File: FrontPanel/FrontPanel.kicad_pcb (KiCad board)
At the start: 2 copper layers, 72 parts, among them SW1 Channel 1, SW10 5, SW11 2, SW12 0, SW13 9, SW14 6, SW15 3, SW16 Backspace, SW17 Voltage 1, SW18 Current 1, SW19 Voltage 2, SW2 Confirm, SW20 Current 2, SW3 Cancel, SW4 Channel 2, SW5 7, SW6 4, SW7 1, SW8 Decimal, SW9 8

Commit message: Fix front panel and routed main regulator
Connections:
- C_DBC_21 pad 1: Net-(Front_Panel2-Pad1) -> Net-(C_DBC_21-Pad1)
- C_DBC_22 pad 2: Net-(Front_Panel2-Pad1) -> Net-(C_DBC_21-Pad1)
- C_DBC_23 pad 1: Net-(Front_Panel2-Pad6) -> Net-(C_DBC_23-Pad1)
- C_DBC_23 pad 2: Net-(C_DBC_23-Pad2) -> Net-(RotaryEncoder+Switch1-PadS2)
- Front_Panel2 pad 1: Net-(Front_Panel2-Pad1) -> Net-(C_DBC_21-Pad1)
- Front_Panel2 pad 13: Net-(SW1-Pad1) -> Net-(SW13-Pad1)
- Front_Panel2 pad 14: Net-(SW10-Pad1) -> Net-(Front_Panel2-Pad14)
- Front_Panel2 pad 15: Net-(SW11-Pad1) -> Net-(Front_Panel2-Pad15)
- Front_Panel2 pad 16: Net-(SW12-Pad1) -> Net-(Front_Panel2-Pad16)
- R1 pad 2: Net-(Front_Panel2-Pad1) -> Net-(C_DBC_21-Pad1)
- R2 pad 2: Net-(Front_Panel2-Pad1) -> Net-(C_DBC_21-Pad1)
- R_DBC_1 pad 1: Net-(C_DBC_1-Pad2) -> Net-(SW13-Pad1)
- R_DBC_10 pad 1: Net-(C_DBC_10-Pad2) -> Net-(Front_Panel2-Pad14)
- R_DBC_11 pad 1: Net-(C_DBC_10-Pad2) -> Net-(Front_Panel2-Pad15)
- R_DBC_12 pad 1: Net-(C_DBC_10-Pad2) -> Net-(Front_Panel2-Pad16)
- R_DBC_13 pad 1: Net-(C_DBC_13-Pad2) -> Net-(SW13-Pad1)
- R_DBC_14 pad 1: Net-(C_DBC_13-Pad2) -> Net-(Front_Panel2-Pad14)
- R_DBC_15 pad 1: Net-(C_DBC_13-Pad2) -> Net-(Front_Panel2-Pad15)
- R_DBC_16 pad 1: Net-(C_DBC_13-Pad2) -> Net-(Front_Panel2-Pad16)
- R_DBC_17 pad 1: Net-(C_DBC_17-Pad2) -> Net-(SW13-Pad1)
- R_DBC_18 pad 1: Net-(C_DBC_17-Pad2) -> Net-(Front_Panel2-Pad14)
- R_DBC_19 pad 1: Net-(C_DBC_17-Pad2) -> Net-(Front_Panel2-Pad15)
- R_DBC_2 pad 1: Net-(C_DBC_1-Pad2) -> Net-(Front_Panel2-Pad14)
- R_DBC_20 pad 1: Net-(C_DBC_17-Pad2) -> Net-(Front_Panel2-Pad16)
- R_DBC_23 pad 1: Net-(C_DBC_23-Pad2) -> Net-(C_DBC_21-Pad1)
- R_DBC_23 pad 2: Net-(Front_Panel2-Pad6) -> Net-(C_DBC_23-Pad1)
- R_DBC_3 pad 1: Net-(C_DBC_1-Pad2) -> Net-(Front_Panel2-Pad15)
- R_DBC_4 pad 1: Net-(C_DBC_1-Pad2) -> Net-(Front_Panel2-Pad16)
- R_DBC_5 pad 1: Net-(C_DBC_5-Pad2) -> Net-(SW13-Pad1)
- R_DBC_6 pad 1: Net-(C_DBC_5-Pad2) -> Net-(Front_Panel2-Pad14)
- R_DBC_7 pad 1: Net-(C_DBC_5-Pad2) -> Net-(Front_Panel2-Pad15)
- R_DBC_8 pad 1: Net-(C_DBC_5-Pad2) -> Net-(Front_Panel2-Pad16)
- R_DBC_9 pad 1: Net-(C_DBC_10-Pad2) -> Net-(SW13-Pad1)
- RotaryEncoder+Switch1 pad C: Net-(Front_Panel2-Pad1) -> Net-(C_DBC_21-Pad1)
- RotaryEncoder+Switch1 pad S2: Net-(Front_Panel2-Pad1) -> Net-(RotaryEncoder+Switch1-PadS2)
- SW1 pad 1: Net-(SW1-Pad1) -> Net-(SW13-Pad1)
- SW10 pad 1: Net-(SW10-Pad1) -> Net-(Front_Panel2-Pad14)
- SW11 pad 1: Net-(SW11-Pad1) -> Net-(Front_Panel2-Pad15)
- SW12 pad 1: Net-(SW12-Pad1) -> Net-(Front_Panel2-Pad16)
- SW13 pad 1: Net-(SW1-Pad1) -> Net-(SW13-Pad1)
- SW14 pad 1: Net-(SW10-Pad1) -> Net-(Front_Panel2-Pad14)
- SW15 pad 1: Net-(SW11-Pad1) -> Net-(Front_Panel2-Pad15)
- SW16 pad 1: Net-(SW12-Pad1) -> Net-(Front_Panel2-Pad16)
- SW17 pad 1: Net-(SW1-Pad1) -> Net-(SW13-Pad1)
- SW18 pad 1: Net-(SW10-Pad1) -> Net-(Front_Panel2-Pad14)
- SW19 pad 1: Net-(SW11-Pad1) -> Net-(Front_Panel2-Pad15)
- SW2 pad 1: Net-(SW10-Pad1) -> Net-(Front_Panel2-Pad14)
- SW20 pad 1: Net-(SW12-Pad1) -> Net-(Front_Panel2-Pad16)
- SW3 pad 1: Net-(SW11-Pad1) -> Net-(Front_Panel2-Pad15)
- SW4 pad 1: Net-(SW12-Pad1) -> Net-(Front_Panel2-Pad16)
- SW5 pad 1: Net-(SW1-Pad1) -> Net-(SW13-Pad1)
- SW6 pad 1: Net-(SW10-Pad1) -> Net-(Front_Panel2-Pad14)
- SW7 pad 1: Net-(SW11-Pad1) -> Net-(Front_Panel2-Pad15)
- SW8 pad 1: Net-(SW12-Pad1) -> Net-(Front_Panel2-Pad16)
- SW9 pad 1: Net-(SW1-Pad1) -> Net-(SW13-Pad1)

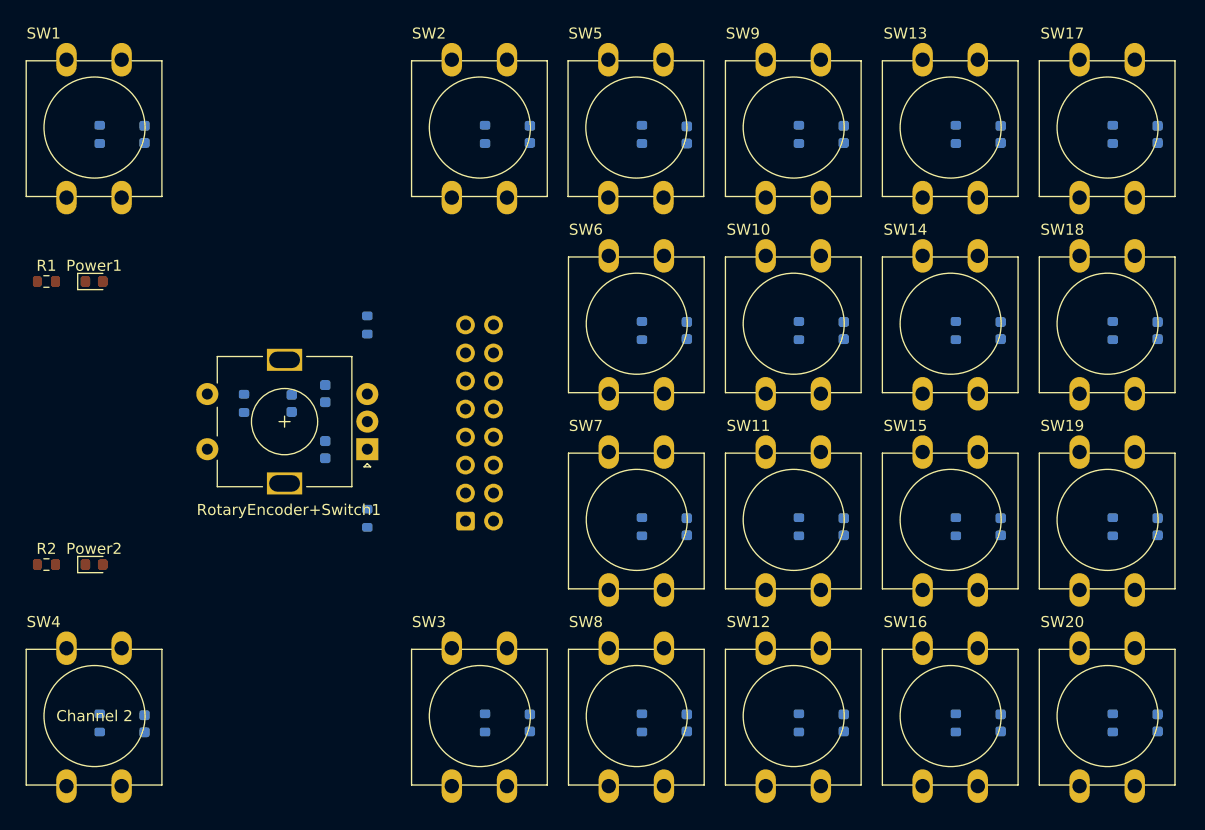
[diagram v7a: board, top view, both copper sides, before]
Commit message: Front panel routing and edge cut
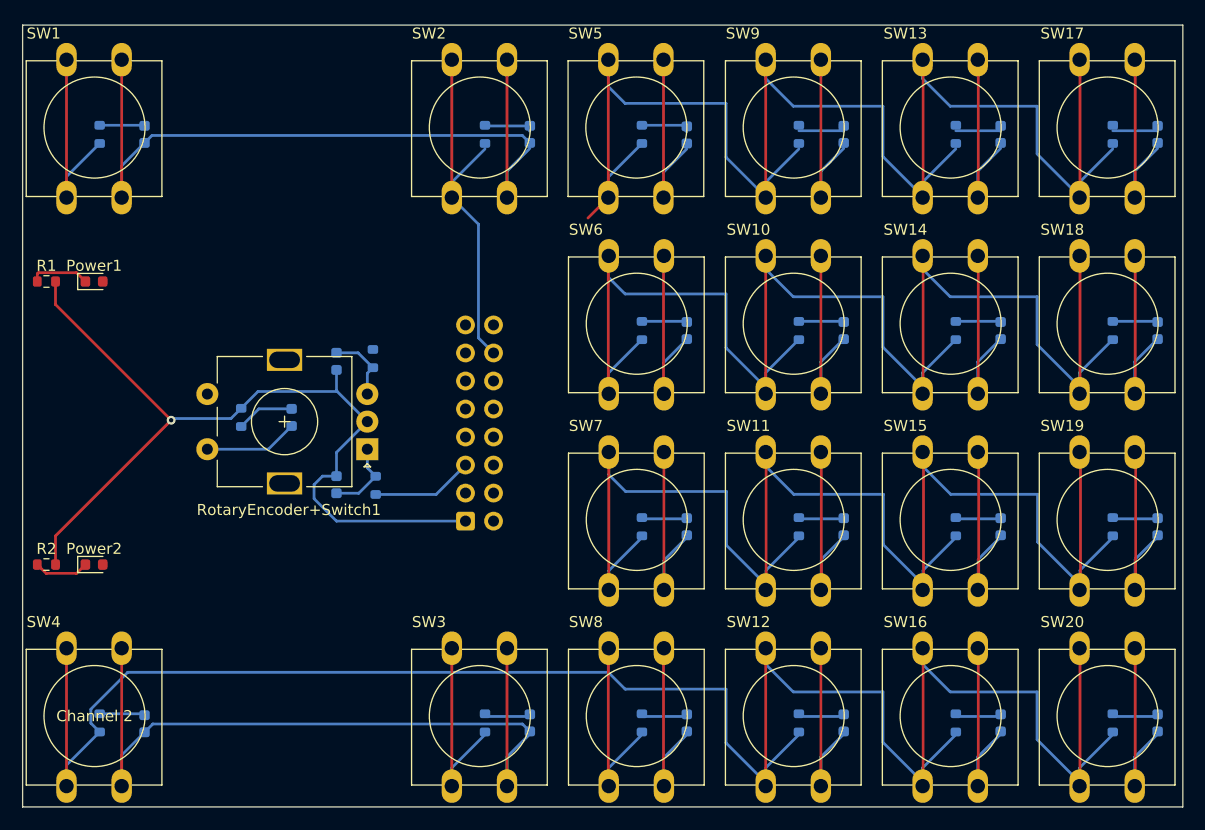
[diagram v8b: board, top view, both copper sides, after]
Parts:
- moved C_DBC_22 3.33 mm to (205.5, 55.6)
- moved C_DBC_21 3.09 mm to (205.5, 44.5)
- moved R_DBC_21 3.09 mm to (208.8, 44.2)
- moved R_DBC_22 3.08 mm to (209.0, 55.7)
- moved R_DBC_23 1.30 mm to (196.8, 49.5), turned to -90 degrees
- moved C_DBC_23 1.27 mm to (201.4, 49.5)
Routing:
- net Net-(Front_Panel2-Pad16): track 0.00 -> 214.0 mm
- net Net-(Front_Panel2-Pad14): track 0.00 -> 179.0 mm
- net Net-(SW13-Pad1): track 0.00 -> 167.8 mm
- net Net-(Front_Panel2-Pad15): track 0.00 -> 163.3 mm
- net Net-(C_DBC_1-Pad2): track 0.00 -> 144.2 mm
- net Net-(C_DBC_21-Pad1): track 0.00 -> 80.6 mm, vias 0 -> 1
- net Net-(C_DBC_10-Pad2): track 0.00 -> 73.3 mm
- net Net-(C_DBC_17-Pad2): track 0.00 -> 73.3 mm
- net Net-(C_DBC_13-Pad2): track 0.00 -> 73.3 mm
- net Net-(C_DBC_5-Pad2): track 0.00 -> 73.1 mm
- net Net-(Front_Panel2-Pad5): track 0.00 -> 9.24 mm
- net Net-(RotaryEncoder+Switch1-PadS2): track 0.00 -> 8.51 mm
- net Net-(C_DBC_22-Pad1): track 0.00 -> 6.96 mm
- net Net-(C_DBC_21-Pad2): track 0.00 -> 6.46 mm
- net Net-(Power1-Pad1): track 0.00 -> 5.43 mm
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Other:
- board outline added: 105.2 x 70.9 mm
